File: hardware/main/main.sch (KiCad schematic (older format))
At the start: 6 parts

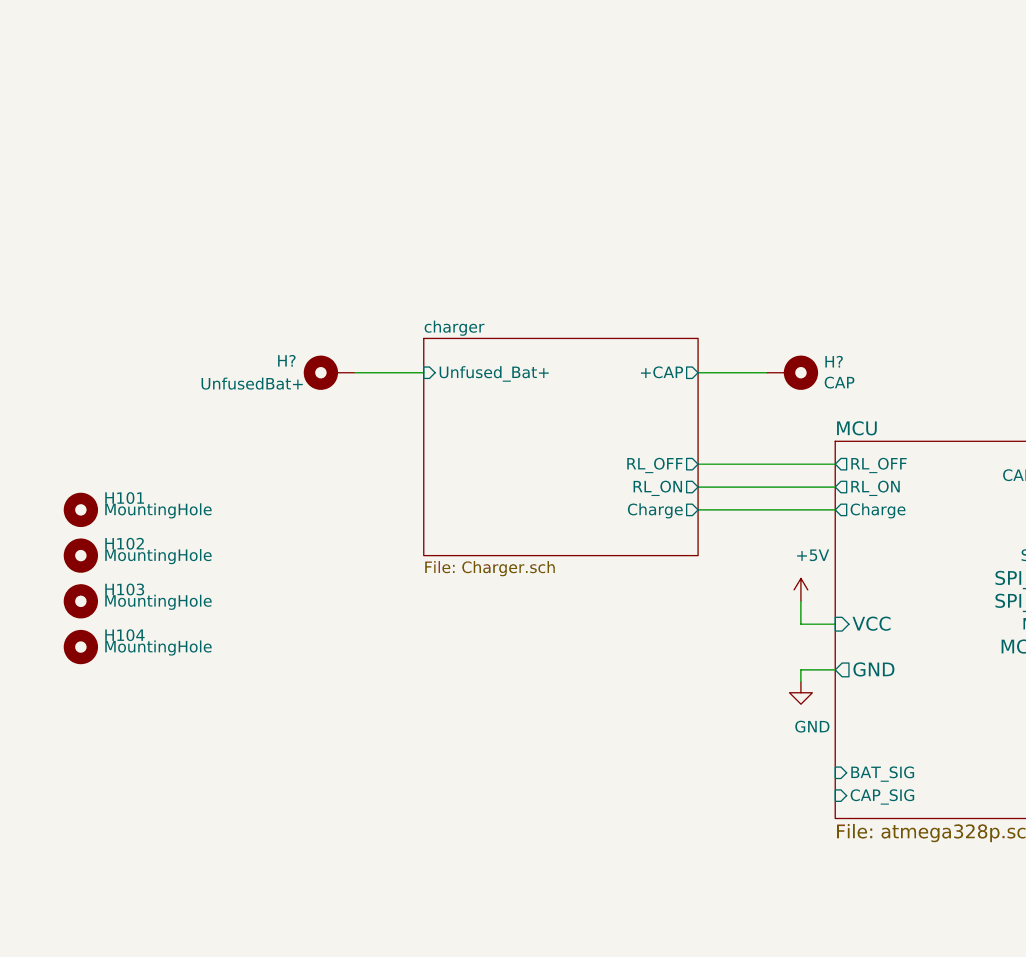
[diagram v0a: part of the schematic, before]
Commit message: Primeira versão do esquematico finalizada Falta DRC
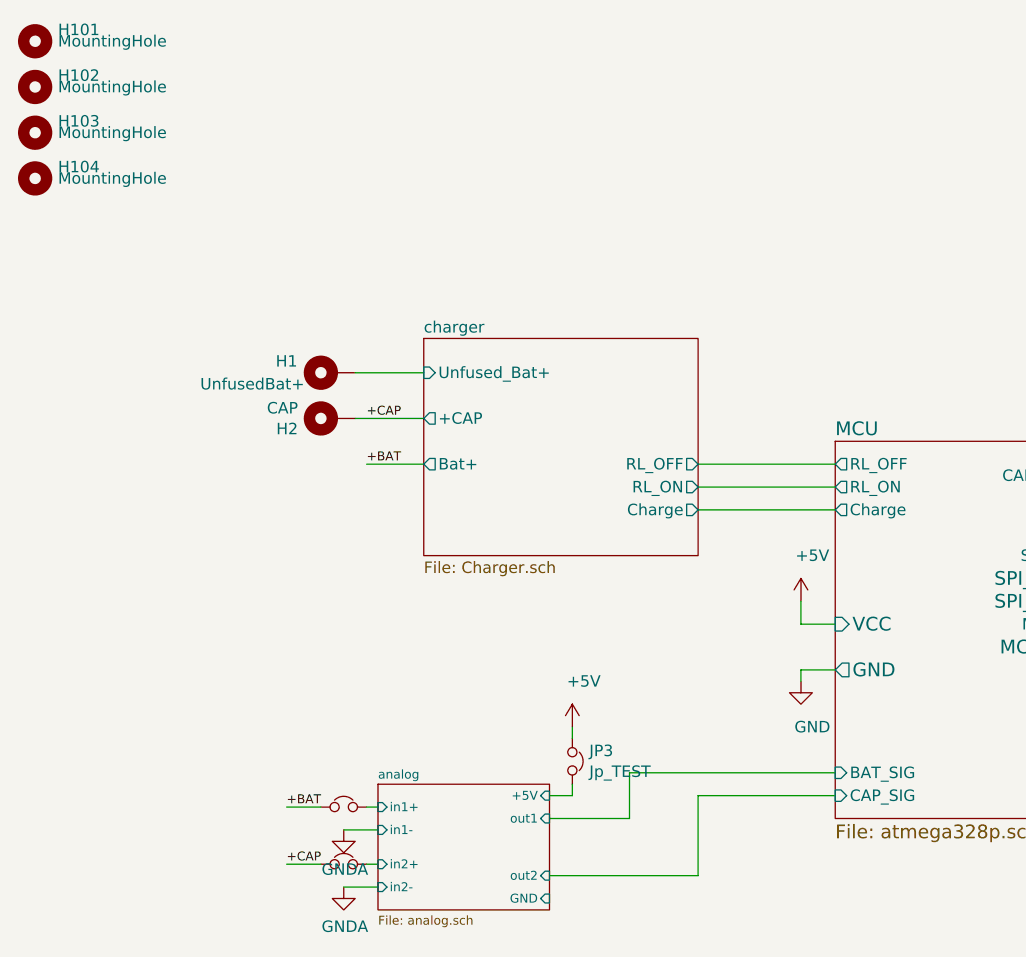
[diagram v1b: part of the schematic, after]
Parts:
- added JP1, JP2, JP3: Jp_TEST, symbol Device:Jumper_NC_Small
- gave numbers to parts that had none: 2
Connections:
- net +5V: now also JP3.1
- net charger/+CAP renamed +CAP
- net +CAP: now also JP2.1
- new net +BAT: JP1.1
- new net analog/+5V: JP3.2
- new net analog/in1+: JP1.2
- new net analog/in2+: JP2.2
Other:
- moved on the sheet: H101, H102, H103, H104, H2
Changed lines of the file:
@@
 EESchema Schematic File Version 4
+LIBS:main-cache
 EELAYER 26 0
 EELAYER END
 $Descr A4 11693 8268
 encoding utf-8
-Sheet 1 7
+Sheet 1 8
 Title ""
 Date ""
@@
 L Mechanical:MountingHole H104
 U 1 1 5BE9AF15
-P 1150 5500
-F 0 "H104" H 1250 5550 50  0000 L CNN
-F 1 "MountingHole" H 1250 5500 50  0000 L CNN
-F 2 "MountingHole:MountingHole_3.2mm_M3" H 1150 5500 50  0001 C CNN
-F 3 "~" H 1150 5500 50  0001 C CNN
-	1    1150 5500
+P 950 3450
+F 0 "H104" H 1050 3500 50  0000 L CNN
+F 1 "MountingHole" H 1050 3450 50  0000 L CNN
+F 2 "MountingHole:MountingHole_3.2mm_M3" H 950 3450 50  0001 C CNN
+F 3 "~" H 950 3450 50  0001 C CNN
+	1    950  3450
 	1    0    0    -1
 $EndComp
@@
 L Mechanical:MountingHole H103
 U 1 1 5BE9BC53
-P 1150 5300
-F 0 "H103" H 1250 5350 50  0000 L CNN
-F 1 "MountingHole" H 1250 5300 50  0000 L CNN
-F 2 "MountingHole:MountingHole_3.2mm_M3" H 1150 5300 50  0001 C CNN
-F 3 "~" H 1150 5300 50  0001 C CNN
-	1    1150 5300
+P 950 3250
+F 0 "H103" H 1050 3300 50  0000 L CNN
+F 1 "MountingHole" H 1050 3250 50  0000 L CNN
+F 2 "MountingHole:MountingHole_3.2mm_M3" H 950 3250 50  0001 C CNN
+F 3 "~" H 950 3250 50  0001 C CNN
+	1    950  3250
 	1    0    0    -1
 $EndComp
@@
 L Mechanical:MountingHole H102
 U 1 1 5BE9BC79
-P 1150 5100
-F 0 "H102" H 1250 5150 50  0000 L CNN
-F 1 "MountingHole" H 1250 5100 50  0000 L CNN
-F 2 "MountingHole:MountingHole_3.2mm_M3" H 1150 5100 50  0001 C CNN
-F 3 "~" H 1150 5100 50  0001 C CNN
-	1    1150 5100
+P 950 3050
+F 0 "H102" H 1050 3100 50  0000 L CNN
+F 1 "MountingHole" H 1050 3050 50  0000 L CNN
+F 2 "MountingHole:MountingHole_3.2mm_M3" H 950 3050 50  0001 C CNN
+F 3 "~" H 950 3050 50  0001 C CNN
+	1    950  3050
 	1    0    0    -1
 $EndComp
@@
 L Mechanical:MountingHole H101
 U 1 1 5BE9BC9F
-P 1150 4900
-F 0 "H101" H 1250 4950 50  0000 L CNN
-F 1 "MountingHole" H 1250 4900 50  0000 L CNN
-F 2 "MountingHole:MountingHole_3.2mm_M3" H 1150 4900 50  0001 C CNN
-F 3 "~" H 1150 4900 50  0001 C CNN
-	1    1150 4900
+P 950 2850
+F 0 "H101" H 1050 2900 50  0000 L CNN
+F 1 "MountingHole" H 1050 2850 50  0000 L CNN
+F 2 "MountingHole:MountingHole_3.2mm_M3" H 950 2850 50  0001 C CNN
+F 3 "~" H 950 2850 50  0001 C CNN
+	1    950  2850
 	1    0    0    -1
 $EndComp
@@
 F4 "RL_OFF" O R 3850 4700 50
 F5 "Unfused_Bat+" I L 2650 4300 50
-F6 "+CAP" O R 3850 4300 50
+F6 "+CAP" O L 2650 4500 50
+F7 "Bat+" O L 2650 4700 50
 $EndSheet
 $Sheet
@@
 	7150 3150 9800 3150
 $Comp
-L Mechanical:MountingHole_Pad H?
+L Mechanical:MountingHole_Pad H1
 U 1 1 5CA207EA
 P 2250 4300
-F 0 "H?" V 2300 4500 50  0000 C CNN
+F 0 "H1" V 2300 4500 50  0000 C CNN
 F 1 "UnfusedBat+" V 2200 4650 50  0000 C CNN
 F 2 "" H 2250 4300 50  0001 C CNN
@@
 	2350 4300 2650 4300
 $Comp
-L Mechanical:MountingHole_Pad H?
+L Mechanical:MountingHole_Pad H2
 U 1 1 5CA21785
-P 4250 4300
-F 0 "H?" V 4204 4450 50  0000 L CNN
-F 1 "CAP" V 4295 4450 50  0000 L CNN
-F 2 "" H 4250 4300 50  0001 C CNN
-F 3 "~" H 4250 4300 50  0001 C CNN
-	1    4250 4300
+P 2250 4500
+F 0 "H2" V 2204 4650 50  0000 L CNN
+F 1 "CAP" V 2295 4650 50  0000 L CNN
+F 2 "" H 2250 4500 50  0001 C CNN
+F 3 "~" H 2250 4500 50  0001 C CNN
+	1    2250 4500
+	0    -1   -1   0
+$EndComp
+Wire Wire Line
+	2350 4500 2650 4500
+Wire Wire Line
+	3850 4900 4450 4900
+Wire Wire Line
+	3850 4800 4450 4800
+Wire Wire Line
+	3850 4700 4450 4700
+$Sheet
+S 2450 6100 750  550
+U 5C9FC045
+F0 "analog" 39
+F1 "analog.sch" 39
+F2 "out1" I R 3200 6250 39
+F3 "+5V" I R 3200 6150 39
+F4 "GND" I R 3200 6600 39
+F5 "in1-" I L 2450 6300 39
+F6 "in1+" I L 2450 6200 39
+F7 "out2" I R 3200 6500 39
+F8 "in2-" I L 2450 6550 39
+F9 "in2+" I L 2450 6450 39
+$EndSheet
+Wire Wire Line
+	3200 6500 3850 6500
+Wire Wire Line
+	3850 6500 3850 6150
+Wire Wire Line
+	3850 6150 4450 6150
+Wire Wire Line
+	3200 6250 3550 6250
+Wire Wire Line
+	3550 6250 3550 6050
+Wire Wire Line
+	3550 6050 4450 6050
+$Comp
+L power:+5V #PWR0112
+U 1 1 5CA11BDD
+P 3300 5850
+F 0 "#PWR0112" H 3300 5700 50  0001 C CNN
+F 1 "+5V" H 3350 6050 50  0000 C CNN
+F 2 "" H 3300 5850 50  0001 C CNN
+F 3 "" H 3300 5850 50  0001 C CNN
+	1    3300 5850
+	1    0    0    -1
+$EndComp
+Wire Wire Line
+	3300 6150 3200 6150
+$Comp
+L Device:Jumper_NC_Small JP3
+U 1 1 5CA139A8
+P 3300 6000
+F 0 "JP3" V 3254 6074 50  0000 L CNN
+F 1 "Jp_TEST" V 3345 6074 50  0000 L CNN
+F 2 "" H 3300 6000 50  0001 C CNN
+F 3 "~" H 3300 6000 50  0001 C CNN
+	1    3300 6000
 	0    1    1    0
 $EndComp
 Wire Wire Line
-	4150 4300 3850 4300
-Wire Wire Line
-	3850 4900 4450 4900
-Wire Wire Line
-	3850 4800 4450 4800
-Wire Wire Line
-	3850 4700 4450 4700
+	3300 5900 3300 5850
+Wire Wire Line
+	3300 6100 3300 6150
+$Comp
+L power:GNDA #PWR0113
+U 1 1 5CA1583E
+P 2300 6300
+F 0 "#PWR0113" H 2300 6050 50  0001 C CNN
+F 1 "GNDA" H 2305 6127 50  0000 C CNN
+F 2 "" H 2300 6300 50  0001 C CNN
+F 3 "" H 2300 6300 50  0001 C CNN
+	1    2300 6300
+	1    0    0    -1
+$EndComp
+Wire Wire Line
+	2300 6300 2450 6300
+$Comp
+L power:GNDA #PWR0114
+U 1 1 5CA1785C
+P 2300 6550
+F 0 "#PWR0114" H 2300 6300 50  0001 C CNN
+F 1 "GNDA" H 2305 6377 50  0000 C CNN
+F 2 "" H 2300 6550 50  0001 C CNN
+F 3 "" H 2300 6550 50  0001 C CNN
+	1    2300 6550
+	1    0    0    -1
+$EndComp
+Wire Wire Line
+	2300 6550 2450 6550
+Text Label 2400 4500 0    39   ~ 0
++CAP
+Text Label 2400 4700 0    39   ~ 0
++BAT
+Wire Wire Line
+	2650 4700 2400 4700
+Text Label 2050 6450 0    39   ~ 0
++CAP
+Text Label 2050 6200 0    39   ~ 0
++BAT
+$Comp
+L Device:Jumper_NC_Small JP1
+U 1 1 5CA254C6
+P 2300 6200
+F 0 "JP1" H 2300 6412 50  0001 C CNN
+F 1 "Jp_TEST" H 2300 6321 50  0001 C CNN
+F 2 "" H 2300 6200 50  0001 C CNN
+F 3 "~" H 2300 6200 50  0001 C CNN
+	1    2300 6200
+	1    0    0    -1
+$EndComp
+Wire Wire Line
+	2050 6200 2200 6200
+Wire Wire Line
+	2400 6200 2450 6200
+$Comp
+L Device:Jumper_NC_Small JP2
+U 1 1 5CA2798A
+P 2300 6450
+F 0 "JP2" H 2300 6662 50  0001 C CNN
+F 1 "Jp_TEST" H 2300 6571 50  0001 C CNN
+F 2 "" H 2300 6450 50  0001 C CNN
+F 3 "~" H 2300 6450 50  0001 C CNN
+	1    2300 6450
+	1    0    0    -1
+$EndComp
+Wire Wire Line
+	2050 6450 2200 6450
+Wire Wire Line
+	2400 6450 2450 6450
 $EndSCHEMATC

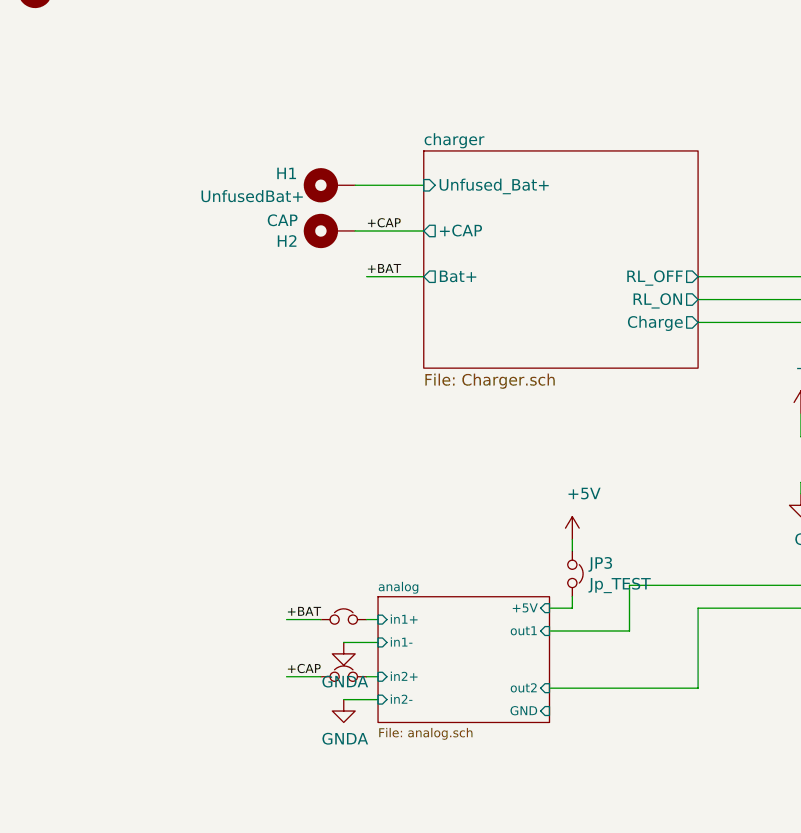
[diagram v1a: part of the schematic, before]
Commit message: O fusivel do sistema foi movido pro GND
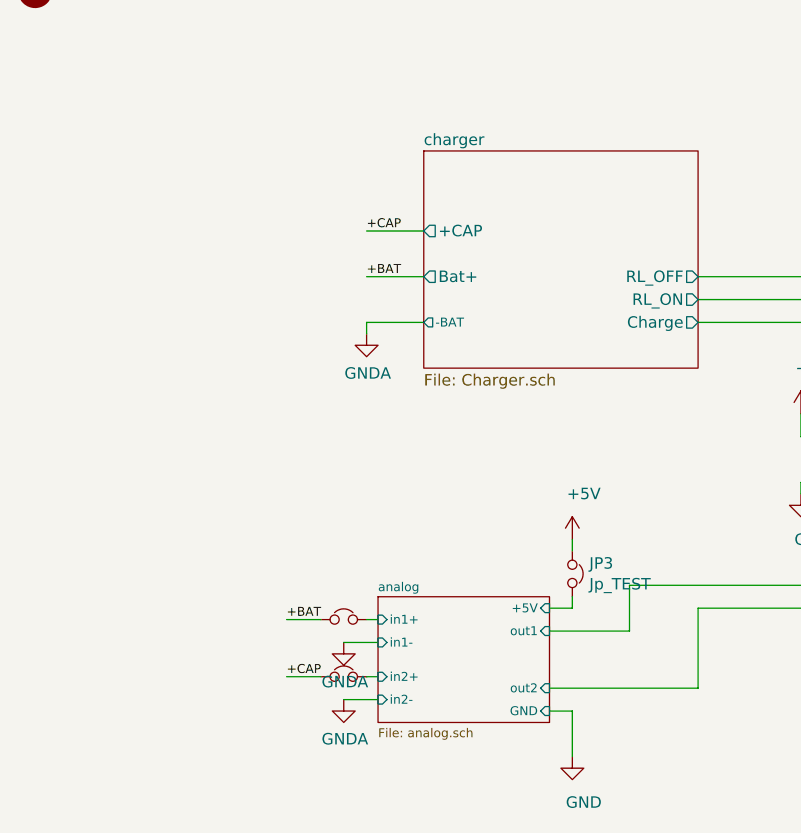
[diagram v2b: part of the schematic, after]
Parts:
- removed H1: UnfusedBat+, symbol Mechanical:MountingHole_Pad
- removed H2: CAP, symbol Mechanical:MountingHole_Pad
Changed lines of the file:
@@
 F3 "RL_ON" O R 3850 4800 50
 F4 "RL_OFF" O R 3850 4700 50
-F5 "Unfused_Bat+" I L 2650 4300 50
-F6 "+CAP" O L 2650 4500 50
-F7 "Bat+" O L 2650 4700 50
+F5 "+CAP" O L 2650 4500 50
+F6 "Bat+" O L 2650 4700 50
+F7 "-BAT" O L 2650 4900 39
 $EndSheet
 $Sheet
@@
 Wire Wire Line
 	7150 3150 9800 3150
-$Comp
-L Mechanical:MountingHole_Pad H1
-U 1 1 5CA207EA
-P 2250 4300
-F 0 "H1" V 2300 4500 50  0000 C CNN
-F 1 "UnfusedBat+" V 2200 4650 50  0000 C CNN
-F 2 "" H 2250 4300 50  0001 C CNN
-F 3 "~" H 2250 4300 50  0001 C CNN
-	1    2250 4300
-	0    -1   -1   0
-$EndComp
-Wire Wire Line
-	2350 4300 2650 4300
-$Comp
-L Mechanical:MountingHole_Pad H2
-U 1 1 5CA21785
-P 2250 4500
-F 0 "H2" V 2204 4650 50  0000 L CNN
-F 1 "CAP" V 2295 4650 50  0000 L CNN
-F 2 "" H 2250 4500 50  0001 C CNN
-F 3 "~" H 2250 4500 50  0001 C CNN
-	1    2250 4500
-	0    -1   -1   0
-$EndComp
-Wire Wire Line
-	2350 4500 2650 4500
 Wire Wire Line
 	3850 4900 4450 4900
@@
 Wire Wire Line
 	2400 6450 2450 6450
+$Comp
+L power:GND #PWR?
+U 1 1 5CA32B5A
+P 3300 6800
+F 0 "#PWR?" H 3300 6550 50  0001 C CNN
+F 1 "GND" H 3350 6600 50  0000 C CNN
+F 2 "" H 3300 6800 50  0001 C CNN
+F 3 "" H 3300 6800 50  0001 C CNN
+	1    3300 6800
+	1    0    0    -1
+$EndComp
+Wire Wire Line
+	3300 6800 3300 6600
+Wire Wire Line
+	3300 6600 3200 6600
+Wire Wire Line
+	2400 4500 2650 4500
+Wire Wire Line
+	2650 4900 2400 4900
+$Comp
+L power:GNDA #PWR?
+U 1 1 5CA4F182
+P 2400 4950
+F 0 "#PWR?" H 2400 4700 50  0001 C CNN
+F 1 "GNDA" H 2405 4777 50  0000 C CNN
+F 2 "" H 2400 4950 50  0001 C CNN
+F 3 "" H 2400 4950 50  0001 C CNN
+	1    2400 4950
+	1    0    0    -1
+$EndComp
+Wire Wire Line
+	2400 4950 2400 4900
 $EndSCHEMATC

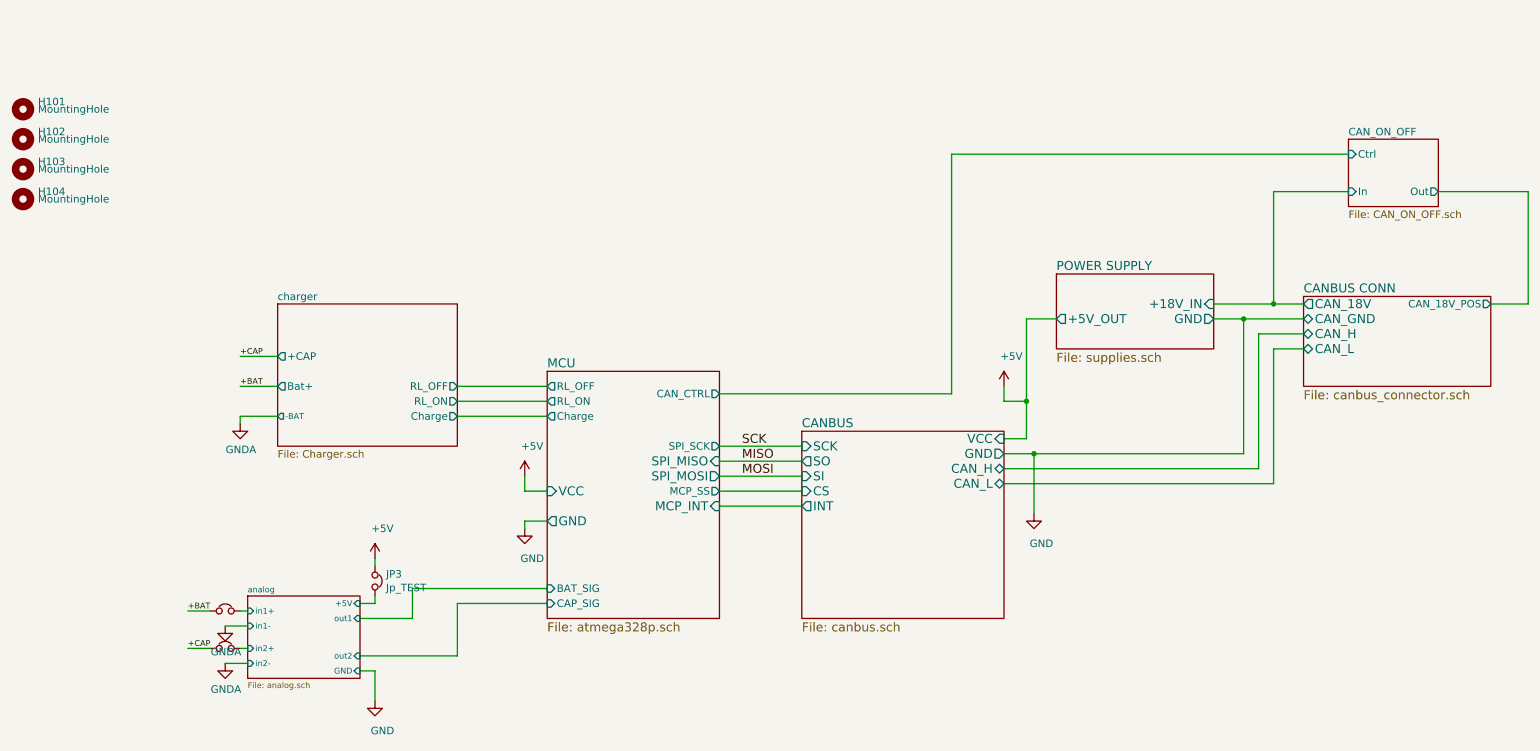
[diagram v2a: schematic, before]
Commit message: Abstração do esquemático modificada para separar as duas placas e mostrar a conexão entre elas na folha principal
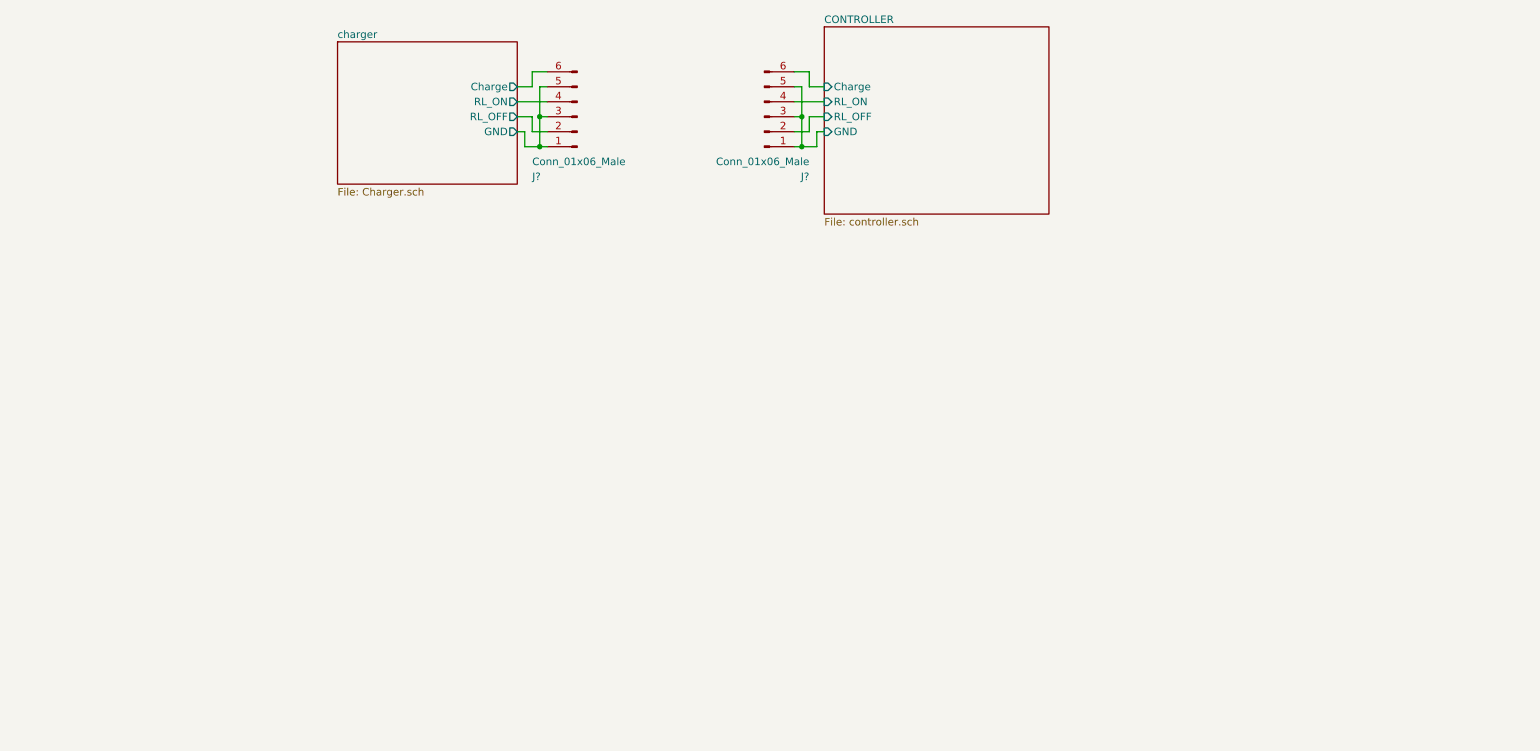
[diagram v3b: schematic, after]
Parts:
- removed H101, H102, H103, H104: MountingHole, MountingHole:MountingHole_3.2mm_M3, symbol Mechanical:MountingHole
- removed JP1, JP2, JP3: Jp_TEST, symbol Device:Jumper_NC_Small
- added J? (x2): Conn_01x06_Male, symbol Connector:Conn_01x06_Male
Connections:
- new net CONTROLLER/Charge: J?.6 (Pin_6)
- new net CONTROLLER/GND: J?.1 (Pin_1), J?.3 (Pin_3), J?.5 (Pin_5)
- new net CONTROLLER/RL_OFF: J?.2 (Pin_2)
- new net CONTROLLER/RL_ON: J?.4 (Pin_4)
- new net charger/Charge: J?.6 (Pin_6)
- new net charger/GND: J?.1 (Pin_1), J?.3 (Pin_3), J?.5 (Pin_5)
- new net charger/RL_OFF: J?.2 (Pin_2)
- new net charger/RL_ON: J?.4 (Pin_4)

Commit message: TO-DO List criada na folha principal
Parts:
- gave numbers to parts that had none: 2
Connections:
- net charger/Charge renamed CHARGER/Charge
- net charger/GND renamed CHARGER/GND
- net charger/RL_OFF renamed CHARGER/RL_OFF
- net charger/RL_ON renamed CHARGER/RL_ON
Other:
- note added: "TO-DO LIST:\n [x] Separar a abstração das duas placas\n\n [x] Criar conexão entre as duas placas\n\n [x] Nomear componentes;\n\n [_] Passar alimentação para o Charger;\n\n [_] Adicionar snubbers para os relés (olhar na simulação);\n\n [_] Passar o condicionamento do sinal para o Charger;\n"
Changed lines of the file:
@@
 S 3050 2400 1200 950
 U 5C9C4D6B
-F0 "charger" 50
+F0 "CHARGER" 50
 F1 "Charger.sch" 50
 F2 "Charge" O R 4250 2700 50
@@
 $EndSheet
 $Comp
-L Connector:Conn_01x06_Male J?
+L Connector:Conn_01x06_Male J101
 U 1 1 5CA76C06
 P 4650 2900
-F 0 "J?" H 4950 3300 50  0000 R CNN
+F 0 "J101" H 4950 3300 50  0000 R CNN
 F 1 "Conn_01x06_Male" H 4950 3200 50  0000 R CNN
 F 2 "" H 4650 2900 50  0001 C CNN
@@
 Connection ~ 4400 3100
 $Comp
-L Connector:Conn_01x06_Male J?
+L Connector:Conn_01x06_Male J102
 U 1 1 5CA80272
 P 5900 2900
-F 0 "J?" H 6200 3300 50  0000 R CNN
+F 0 "J102" H 6200 3300 50  0000 R CNN
 F 1 "Conn_01x06_Male" H 6200 3200 50  0000 R CNN
 F 2 "" H 5900 2900 50  0001 C CNN
@@
 	6250 3000 6300 3000
 Connection ~ 6150 3100
+Text Notes 4400 4750 0    50   ~ 0
+TO-DO LIST:\n  [x] Separar a abstração das duas placas\n\n  [x] Criar conexão entre as duas placas\n\n  [x] Nomear componentes;\n\n  [_] Passar alimentação para o Charger;\n\n  [_] Adicionar snubbers para os relés (olhar na simulação);\n\n  [_] Passar o condicionamento do sinal para o Charger;\n
 $EndSCHEMATC
